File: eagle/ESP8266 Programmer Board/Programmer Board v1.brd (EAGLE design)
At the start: 160 x 100 mm, 11 parts, among them J1 FTDI, J2 DCJ0202, U1 LM7833

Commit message: Updating switches
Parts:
- added D2: PROG, SparkFun-LED:LED3MM
- C1: value (none) -> 0.1uF
- C2: value (none) -> 10uF; device SparkFun-Capacitors:CAP-PTH-SMALL-KIT -> SparkFun-Capacitors:CPOL-RADIAL-10UF-25V-KIT
- J1: device SparkFun-Connectors:1X06_LONGPADS -> SparkFun-Connectors:FTDI_BASIC
- S2: value PROG -> (none); device SparkFun-Electromechanical:SWITCH-SPDT -> SparkFun-Electromechanical:EG2211
- moved J1 115.1 mm to (73.7, 19.1), turned to 270 degrees
- moved D1 98.8 mm to (55.9, 27.9)
- moved C2 77.5 mm to (33.0, 7.62), turned to 90 degrees
- moved R2 69.6 mm to (19.1, 30.5), turned to 180 degrees
- moved JP1 67.1 mm to (41.9, 14.0), turned to 270 degrees
- moved C1 61.3 mm to (20.3, 8.89), turned to 270 degrees
- moved U1 46.4 mm to (26.7, 14.0)
- moved S2 43.3 mm to (7.62, 33.0), turned to 270 degrees
- moved R1 41.7 mm to (15.2, 22.9), turned to 90 degrees
- moved S1 38.2 mm to (7.62, 22.2), turned to 90 degrees
- moved J2 32.5 mm to (6.35, 11.4)
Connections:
- removed net 3V3: JP1.7
- removed net CH_PD: JP1.3, S2.3
- removed net N$1: D1.K, R2.P$2
- new net N$3: D1.K, S2.P2-TA
- new net N$4: R2.P$2, S2.P2
- net +3V3: now also D2.A, JP1.3, JP1.7
- net GND: now also J1.GND, R2.P$1, S2.P1; no longer J1.6, S2.2
- net GPIO0: now also S2.P1-TB
- net N$2: now also D2.K, S2.P2-TB; no longer R2.P$1, S2.1
- net RX: now also J1.TXO; no longer J1.3
- net TX: now also J1.RXI; no longer J1.2
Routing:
- net GND: track 0.00 -> 148.2 mm
- net +3V3: track 0.00 -> 82.9 mm
- net GPIO0: track 0.00 -> 62.1 mm
- net RST: track 0.00 -> 33.4 mm
- net VCC: track 0.00 -> 24.9 mm
- net N$4: track 0.00 -> 9.16 mm
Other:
- board size 160 x 100 mm -> 78.7 x 49.2 mm

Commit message: Board routing
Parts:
- S2: device SparkFun-Electromechanical:EG2211 -> switch:A68-A31
- moved S2 56.1 mm to (63.5, 27.9), turned to 0 degrees
- moved R2 34.5 mm to (53.3, 26.7), turned to 90 degrees
- moved D2 23.4 mm to (45.7, 33.0)
- moved D1 10.5 mm to (45.7, 25.4)
- moved J2 5.68 mm to (11.4, 8.89), turned to 270 degrees
- moved S1 5.08 mm to (7.62, 27.3)
- moved C1 3.81 mm to (20.3, 5.08), turned to 180 degrees
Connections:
- net GND: now also S2.2; no longer S2.P1
- net GPIO0: now also S2.3; no longer S2.P1-TB
- net N$2: now also S2.6; no longer S2.P2-TB
- net N$3: now also S2.4; no longer S2.P2-TA
- net N$4: now also S2.5; no longer S2.P2
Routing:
- net GND: track 148.2 -> 7.62 mm, vias 0 -> 2
- net TX: track 0.00 -> 46.4 mm
- net +3V3: track 82.9 -> 115.4 mm
- net RX: track 0.00 -> 32.1 mm
- net GPIO0: track 62.1 -> 32.6 mm
- net N$2: track 0.00 -> 22.6 mm
- net N$3: track 0.00 -> 16.1 mm
- net VCC: track 24.9 -> 17.2 mm
- net N$4: track 9.16 -> 13.8 mm
- net RST: track 33.4 -> 35.6 mm
- added copper zone on layer 16, net GND
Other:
- board size 78.7 x 49.2 mm -> 80 x 36.5 mm

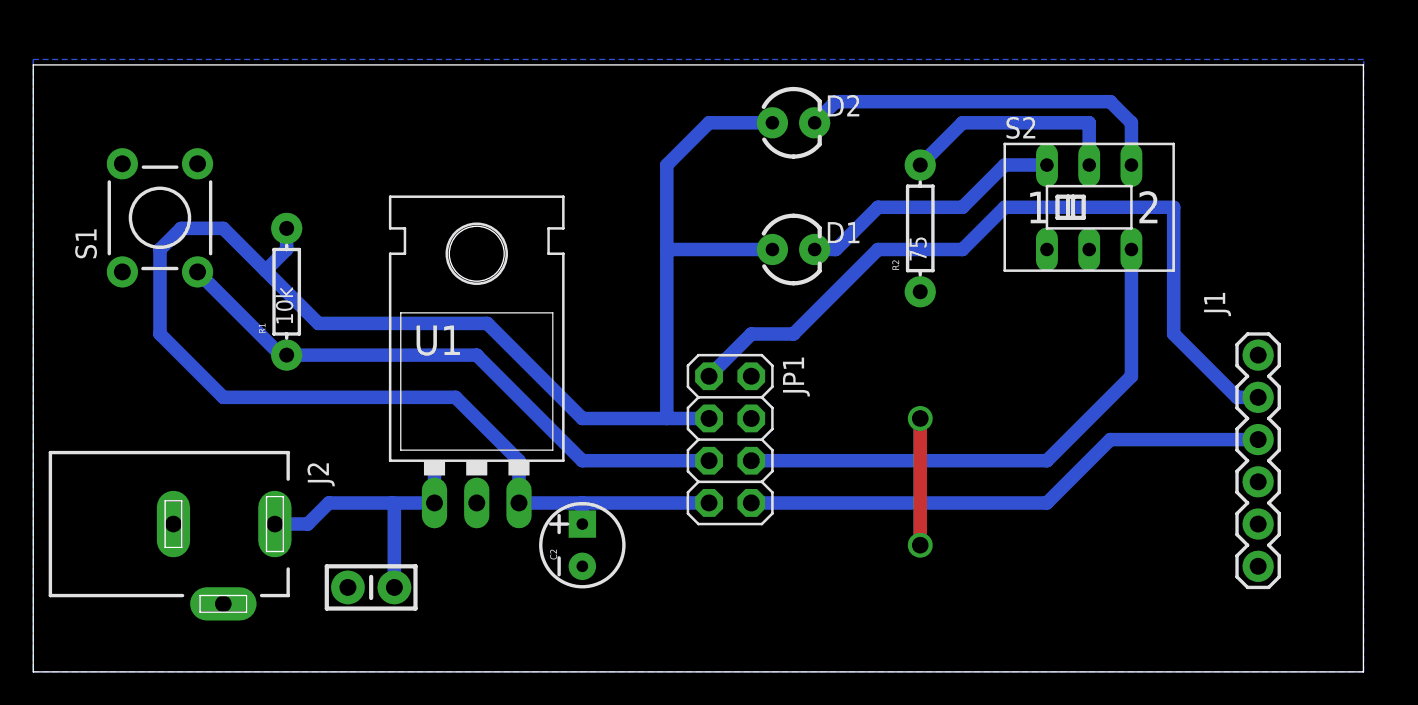
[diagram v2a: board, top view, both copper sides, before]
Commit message: Power Supply regulator ref design
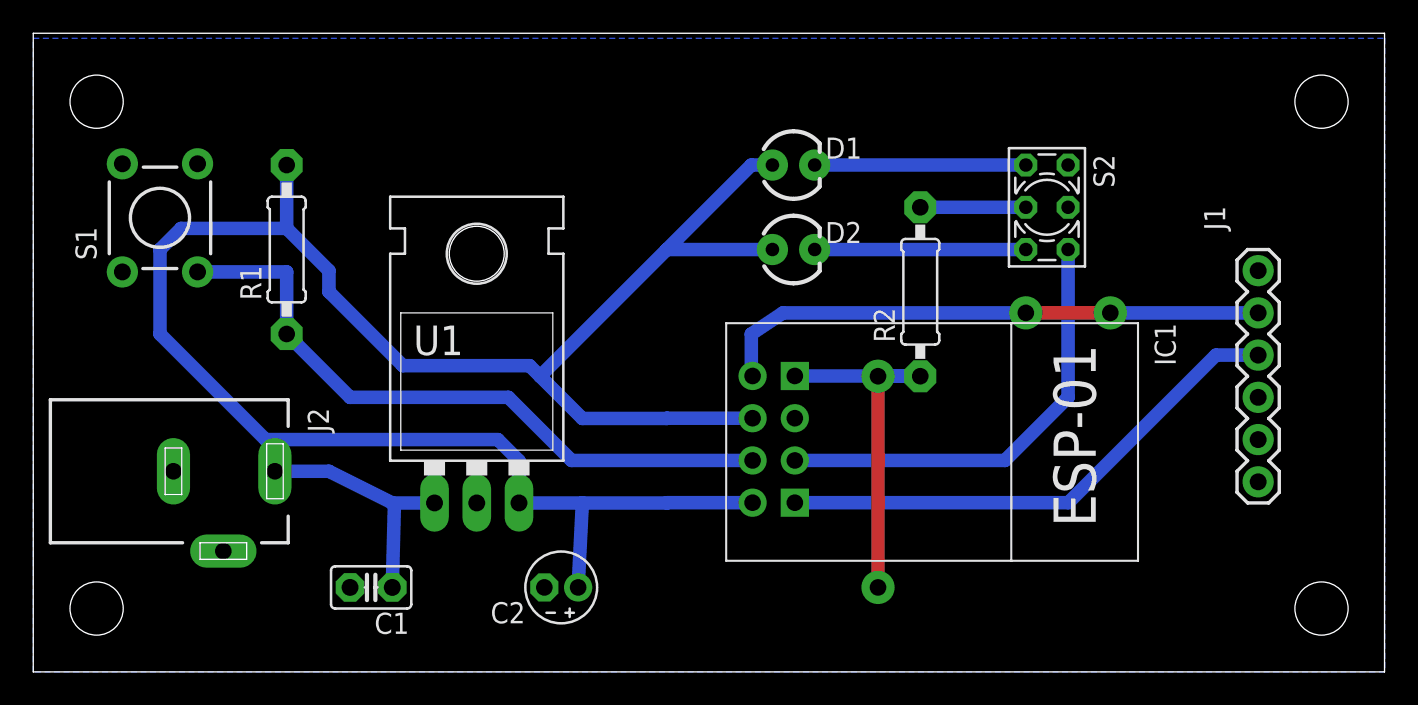
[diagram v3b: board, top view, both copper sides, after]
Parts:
- removed JP1: ESP8266, adafruit:2X04
- added IC1: ESP01, esp8266modules:ESP01
- C1: device SparkFun-Capacitors:CAP-PTH-SMALL-KIT -> rcl:C025-025X050
- C2: device SparkFun-Capacitors:CPOL-RADIAL-10UF-25V-KIT -> rcl:E2-4
- R1, R2: device SparkFun-Resistors:AXIAL-0.3 -> rcl:0207/10
- S2: device switch:A68-A31 -> switch-misc:9450-2
- moved D2 7.62 mm to (45.7, 25.4)
- moved D1 5.08 mm to (45.7, 30.5)
- moved J1 5.08 mm to (73.7, 24.1)
- moved R2 3.81 mm to (53.3, 22.9)
- moved J2 3.17 mm to (11.4, 12.1)
- moved C2 2.84 mm to (31.8, 5.08), turned to 180 degrees
- moved R1 2.54 mm to (15.2, 25.4)
- moved S2 2.54 mm to (61.0, 27.9), turned to 270 degrees
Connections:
- removed net GPIO2: JP1.4
- removed net N$4: R2.P$2, S2.5
- new net N$1: D2.K, S2.3
- net +3V3: now also C2.+, IC1.CH_PD, IC1.VCC, R1.2; no longer C2.1, JP1.3, JP1.7, R1.P$2
- net GND: now also C2.-, IC1.GND, R2.1, S2.5; no longer C2.2, JP1.2, R2.P$1, S2.2
- net GPIO0: now also IC1.GPIO0, S2.6; no longer JP1.6, S2.3
- net N$2: now also R2.2, S2.2; no longer D2.K, S2.6
- net N$3: now also S2.1; no longer S2.4
- net RST: now also IC1.RST, R1.1; no longer JP1.5, R1.P$1
- net RX: now also IC1.RX; no longer JP1.8
- net TX: now also IC1.TX; no longer JP1.1
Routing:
- net N$2: track 22.6 -> 6.35 mm
- net GND: track 7.62 -> 22.8 mm
- net N$4: track 13.8 -> 0.00 mm
- net TX: track 46.4 -> 33.4 mm, vias 0 -> 2
- net N$1: track 0.00 -> 12.7 mm
- net +3V3: track 115.4 -> 122.5 mm
- net GPIO0: track 32.6 -> 26.9 mm
- net RST: track 35.6 -> 40.3 mm
- net N$3: track 16.1 -> 12.7 mm
- net RX: track 32.1 -> 31.5 mm
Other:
- board size 80 x 36.5 mm -> 81.3 x 38.4 mm
